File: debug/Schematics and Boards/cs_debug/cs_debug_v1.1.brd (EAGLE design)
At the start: 81.3 x 62.2 mm, 217 parts, among them J1 J-JTAG-CORTEX_SMD, J19 Solar, J3 HIROSE-DF40_50-PIN_CONNECTORS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, J5 J-WURTH-USBC, Q10 2N7002P, Q3 FDN340P, Q4 2N7002P, Q5 FDN340P, Q6 2N7002P, Q7 FDN340P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

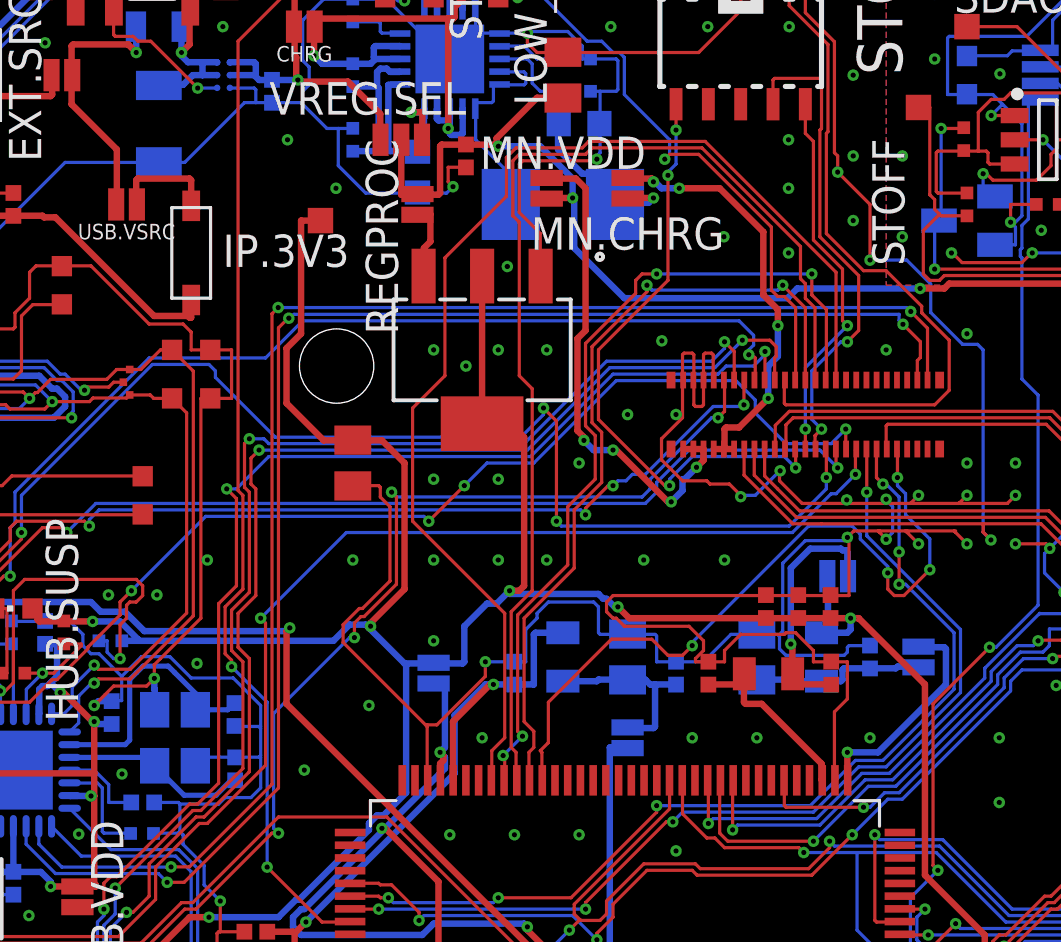
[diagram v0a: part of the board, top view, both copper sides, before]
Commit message: DBG: move component from screw hole and regen gerbers
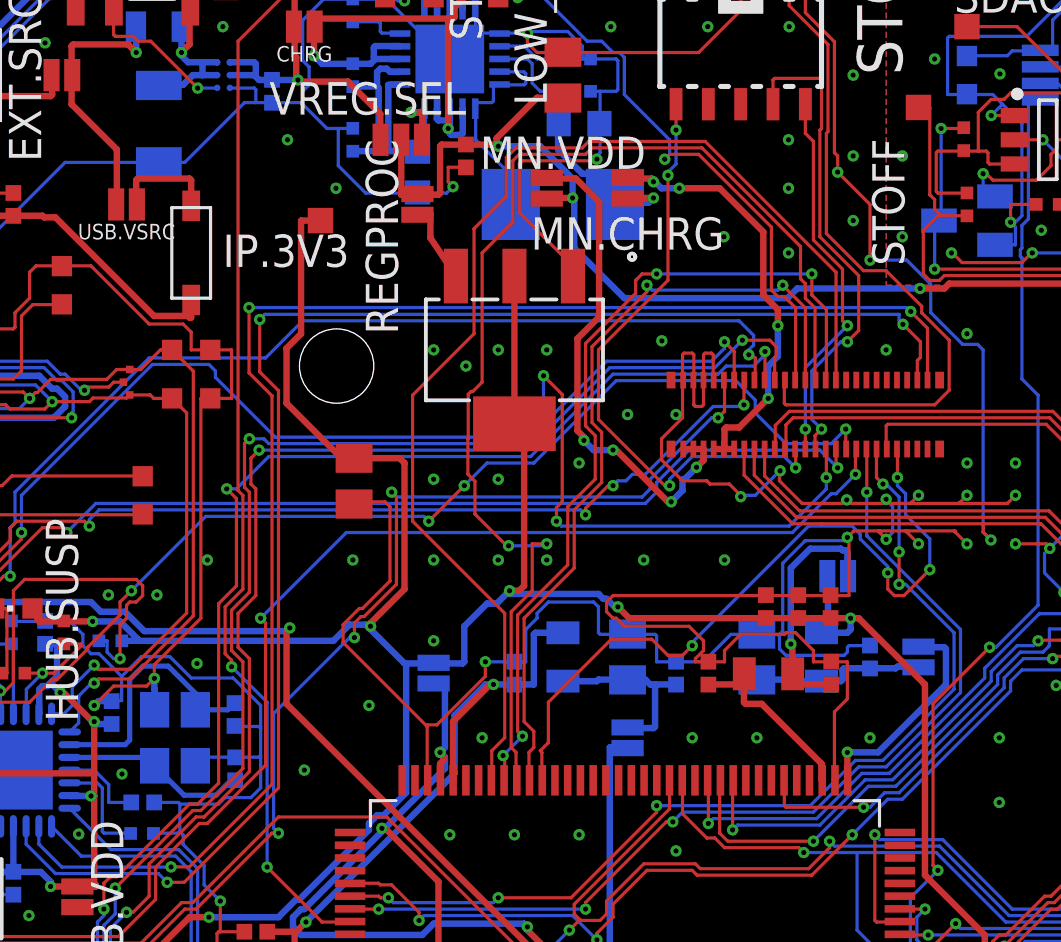
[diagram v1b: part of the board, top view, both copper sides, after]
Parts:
- moved U2 1.27 mm to (10.2, 44.5)
- moved C2 0.71 mm to (3.86, 39.3)
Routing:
- net MAIN_GPIO2: track 43.7 -> 47.0 mm, vias 0 -> 2
- net MAIN_GPIO4/SERCOM_P0: track 56.9 -> 59.6 mm
- net MAIN_USB_DATA_N: track 58.3 -> 59.7 mm
- net MAIN_USB_DATA_P: track 58.4 -> 59.7 mm
- net 3V3_INSTR_PROC: track 197.7 -> 196.7 mm
- net DGND: vias 174 -> 173

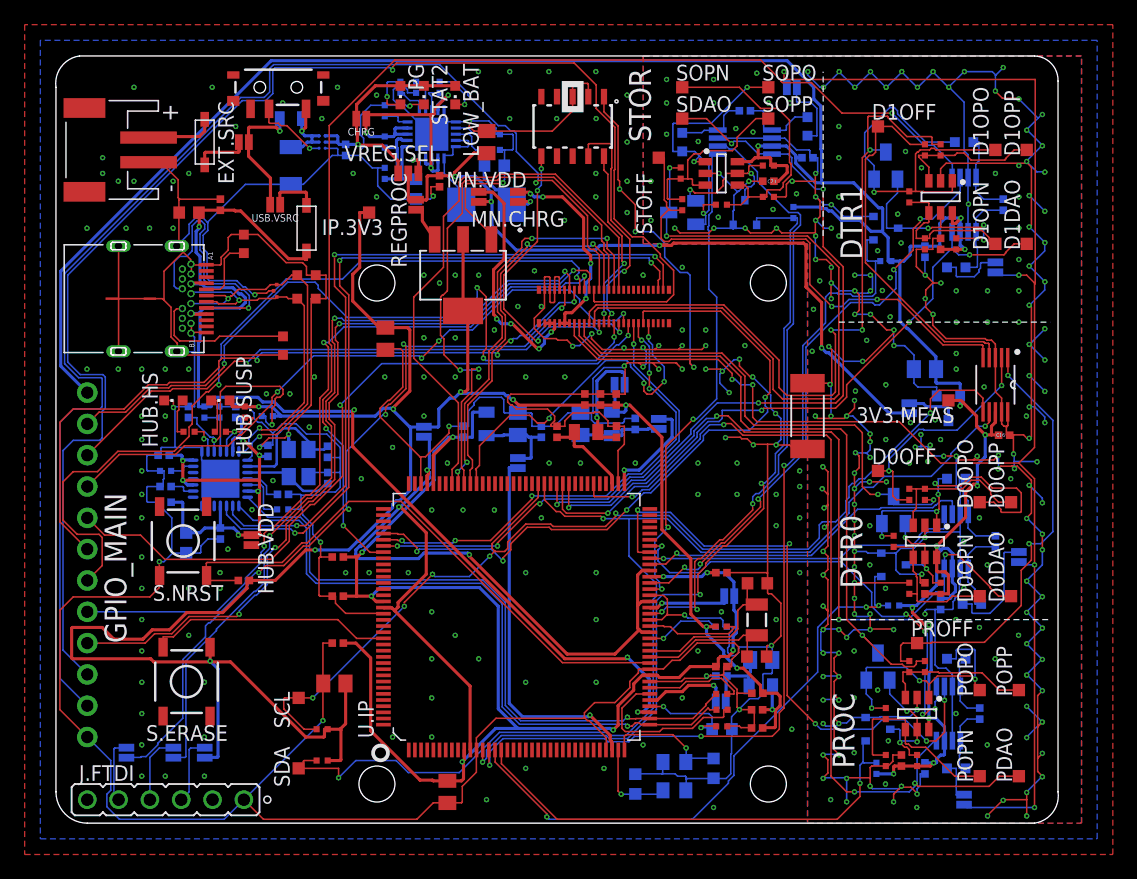
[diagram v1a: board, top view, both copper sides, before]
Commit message: DBG: Increase holes sizes for snap-lock inter-board connectors
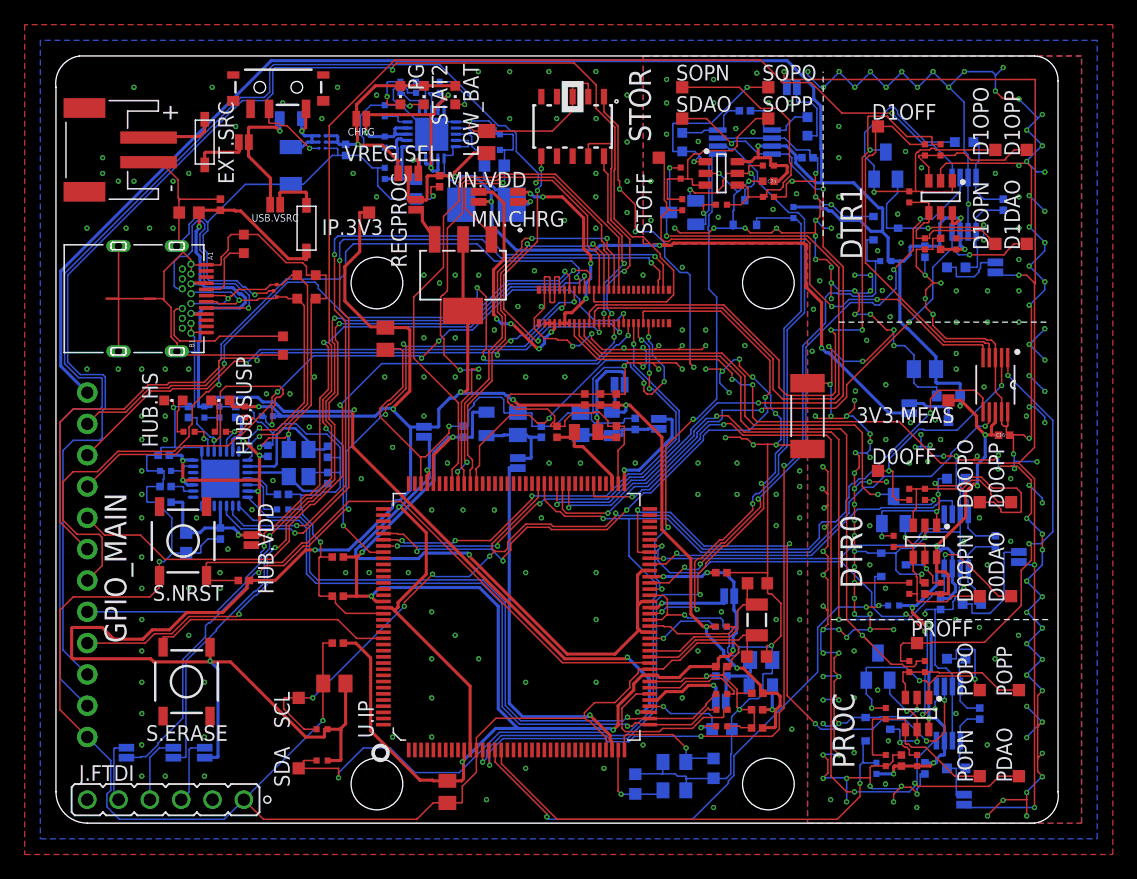
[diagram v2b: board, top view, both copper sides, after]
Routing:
- net MAIN_TRACE_D0/GPIO13: track 65.5 -> 67.7 mm
- net MAIN_USB_DATA_P: track 59.7 -> 61.7 mm
- net MAIN_USB_DATA_N: track 59.7 -> 61.7 mm
- net INSTR_PROC_I2C_SDA: track 96.0 -> 97.1 mm
- net 3V3_INSTR_PROC: track 196.7 -> 197.6 mm

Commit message: DBG: Replace bias resistors of current measurement w/ correct part
And regenerate the CAM files.
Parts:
- R16, R20, R24, R25, R29, R36, R40, R56: device Resistors:R0402 -> Resistors:R0603
- moved R36 0.36 mm to (47.6, 46.6)
- moved R29 0.36 mm to (46.0, 19.0)
- moved R25 0.33 mm to (46.0, 26.7)
- moved R20 0.30 mm to (44.1, 5.08)
- moved R40 0.26 mm to (27.7, 50.2)
- moved R56 0.15 mm to (35.0, 50.6)
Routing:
- net CM_DTR1_OPAMP_P: track 11.9 -> 11.2 mm
- net CM_DTR0_OPAMP_N: track 12.0 -> 12.7 mm
- net CM_OPAMP_P3: track 12.5 -> 13.2 mm
- net AGND: track 420.4 -> 421.0 mm
